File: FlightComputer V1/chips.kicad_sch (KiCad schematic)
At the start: 5 parts, among them U1 GYU-521, U3 W25Q64, U4 GY-BMP280, U5 Micro-SD-Card-Holder

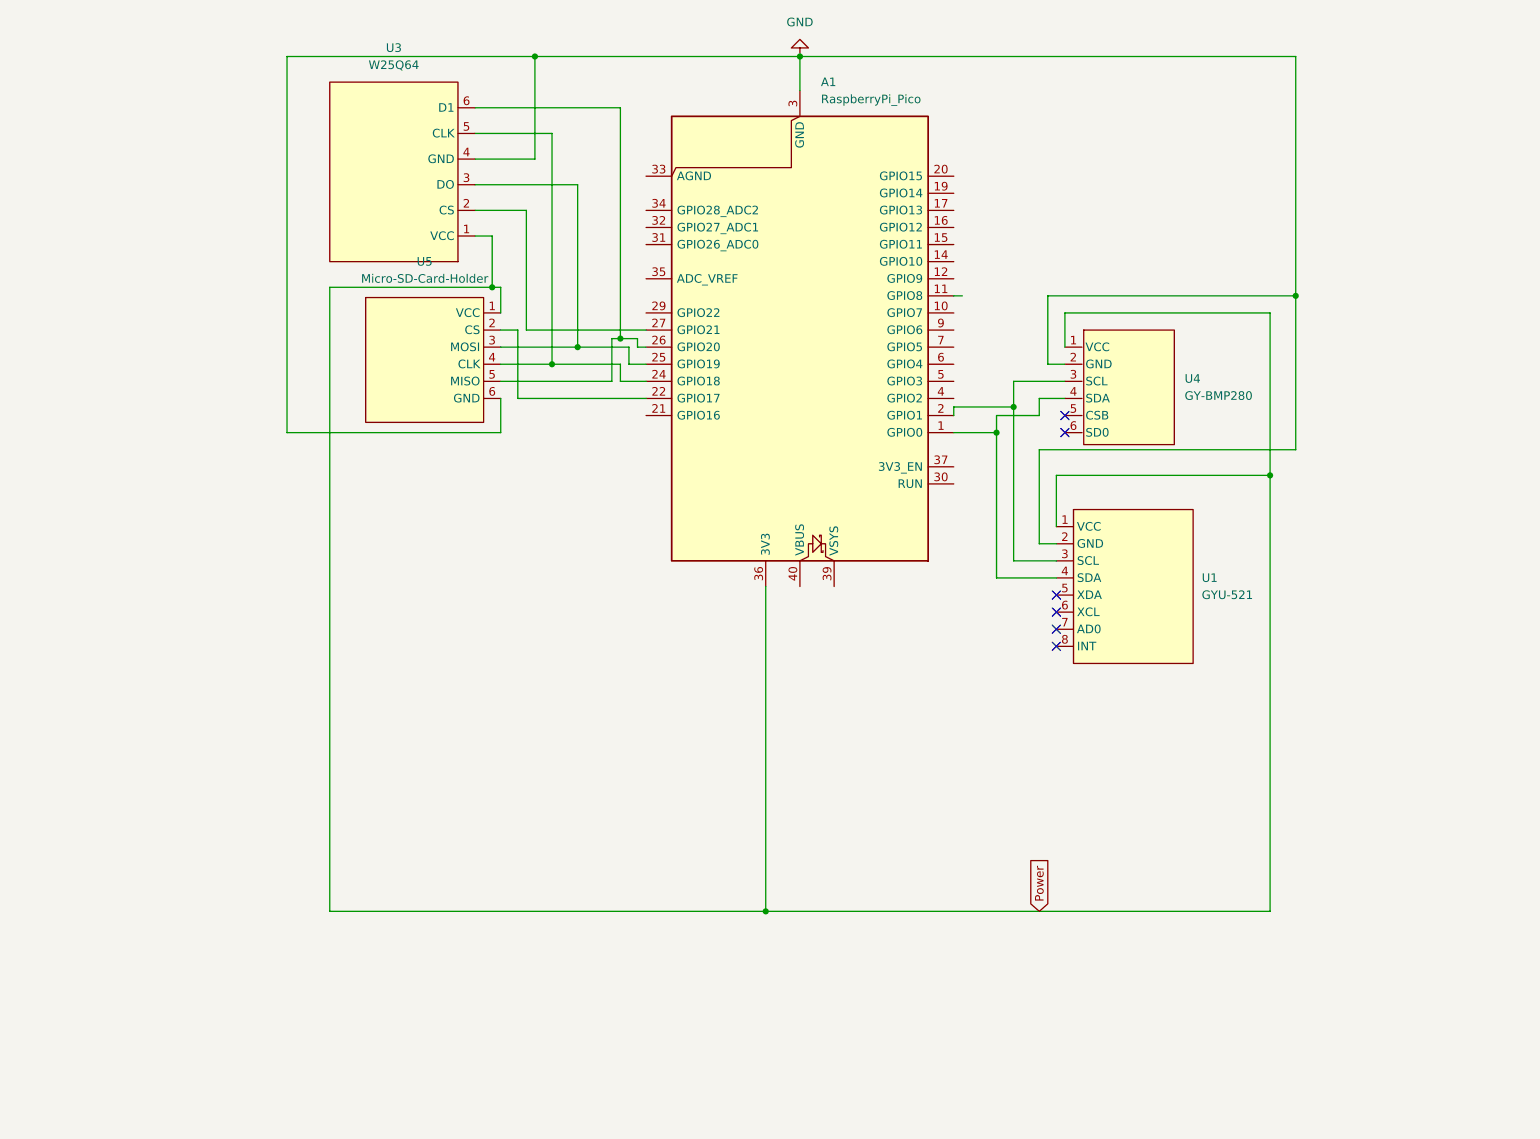
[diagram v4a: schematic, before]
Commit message: Tidy up chips sheet
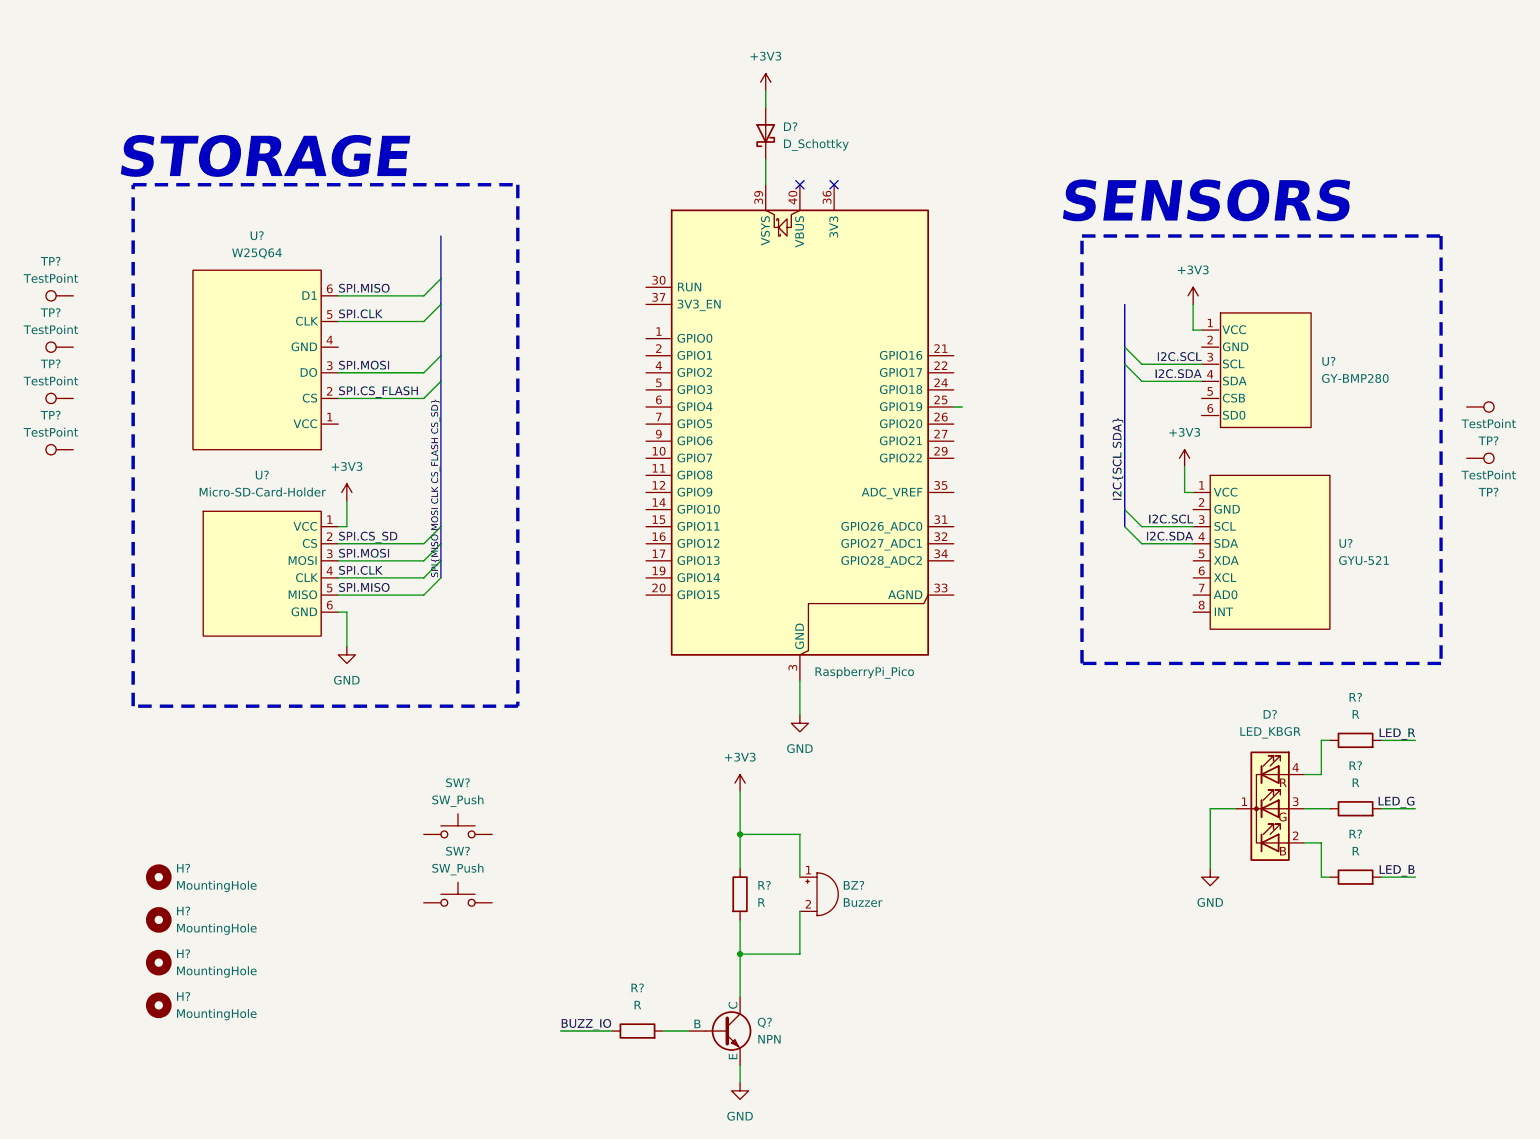
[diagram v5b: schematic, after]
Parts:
- added BZ?: Buzzer, symbol Device:Buzzer
- added D?: D_Schottky, symbol Device:D_Schottky
- added D?: LED_KBGR, symbol Device:LED_KBGR
- added H? (x4): MountingHole, symbol Mechanical:MountingHole
- added Q?: NPN, symbol Simulation_SPICE:NPN
- added R? (x5): R, symbol Device:R
- added SW? (x2): SW_Push, symbol Switch:SW_Push
- added TP? (x6): TestPoint, symbol Connector:TestPoint
- renumbered A1 to A?, U5 to U?, U1 to U?, U3 to U?, U4 to U?
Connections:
- net GND: now also D?.1 (K), Q?.3 (E); no longer U?.2 (GND), U?.2 (GND), U?.4 (GND)
- net at A?.22 (GPIO17): no longer U?.2 (CS)
- net SPI.MOSI: now reaches U?.3 (DO), U?.3 (MOSI)
- net SPI.MOSI: no longer A?.25 (GPIO19)
- net SPI.CLK: now reaches U?.4 (CLK), U?.5 (CLK)
- net SPI.CLK: no longer A?.24 (GPIO18)
- net SPI.MISO: now reaches U?.5 (MISO), U?.6 (D1)
- net SPI.MISO: no longer A?.26 (GPIO20)
- net I2C.SCL: now reaches U?.3 (SCL), U?.3 (SCL)
- net I2C.SCL: no longer A?.2 (GPIO1)
- net I2C.SDA: now reaches U?.4 (SDA), U?.4 (SDA)
- net I2C.SDA: no longer A?.1 (GPIO0)
- net at A?.27 (GPIO21): no longer U?.2 (CS)
- net at A?.39 (VSYS): now also D?.1 (K)
- net Power renamed +3V3
- net +3V3: now also BZ?.1 (+), D?.2 (A), R?.1; no longer A?.36 (3V3), U?.1 (VCC)
- new net: D?.4 (RA), R?.1
- new net: D?.3 (GA), R?.1
- new net: BZ?.2 (-), Q?.1 (C), R?.2
- new net: Q?.2 (B), R?.2
- new net: D?.2 (BA), R?.1
- new net BUZZ_IO: R?.1
- new net LED_B: R?.2
- new net LED_G: R?.2
- new net LED_R: R?.2
- new net SPI.CS_FLASH: U?.2 (CS)
- new net SPI.CS_SD: U?.2 (CS)
- no-connect marks 6 -> 2
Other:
- note added: "SENSORS"
- note added: "STORAGE"
- moved on the sheet: U?
